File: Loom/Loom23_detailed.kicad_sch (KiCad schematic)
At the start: 7 parts

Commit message: Changes to the injector numbering
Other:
- sheet Relaybox indicators renamed Relaybox indicators (relays)
- added sheet Relaybox indicators (ECU) (Relaybox Indicator LEDs/relaybox_indicator_leds.kicad_sch)
- note added: "High impedance injectors, no extra resistors needed."
- note added: "Note: there is only one relaybox indicator board, but it can be connected to either the relays or the ECU, so it is included twice in this diagram"
- note removed: "Assuming cylinder 1 is on the left High impedance injectors, no extra resistors needed."
- note removed: "CAN Bus"
- note removed: "CAN Sensors"

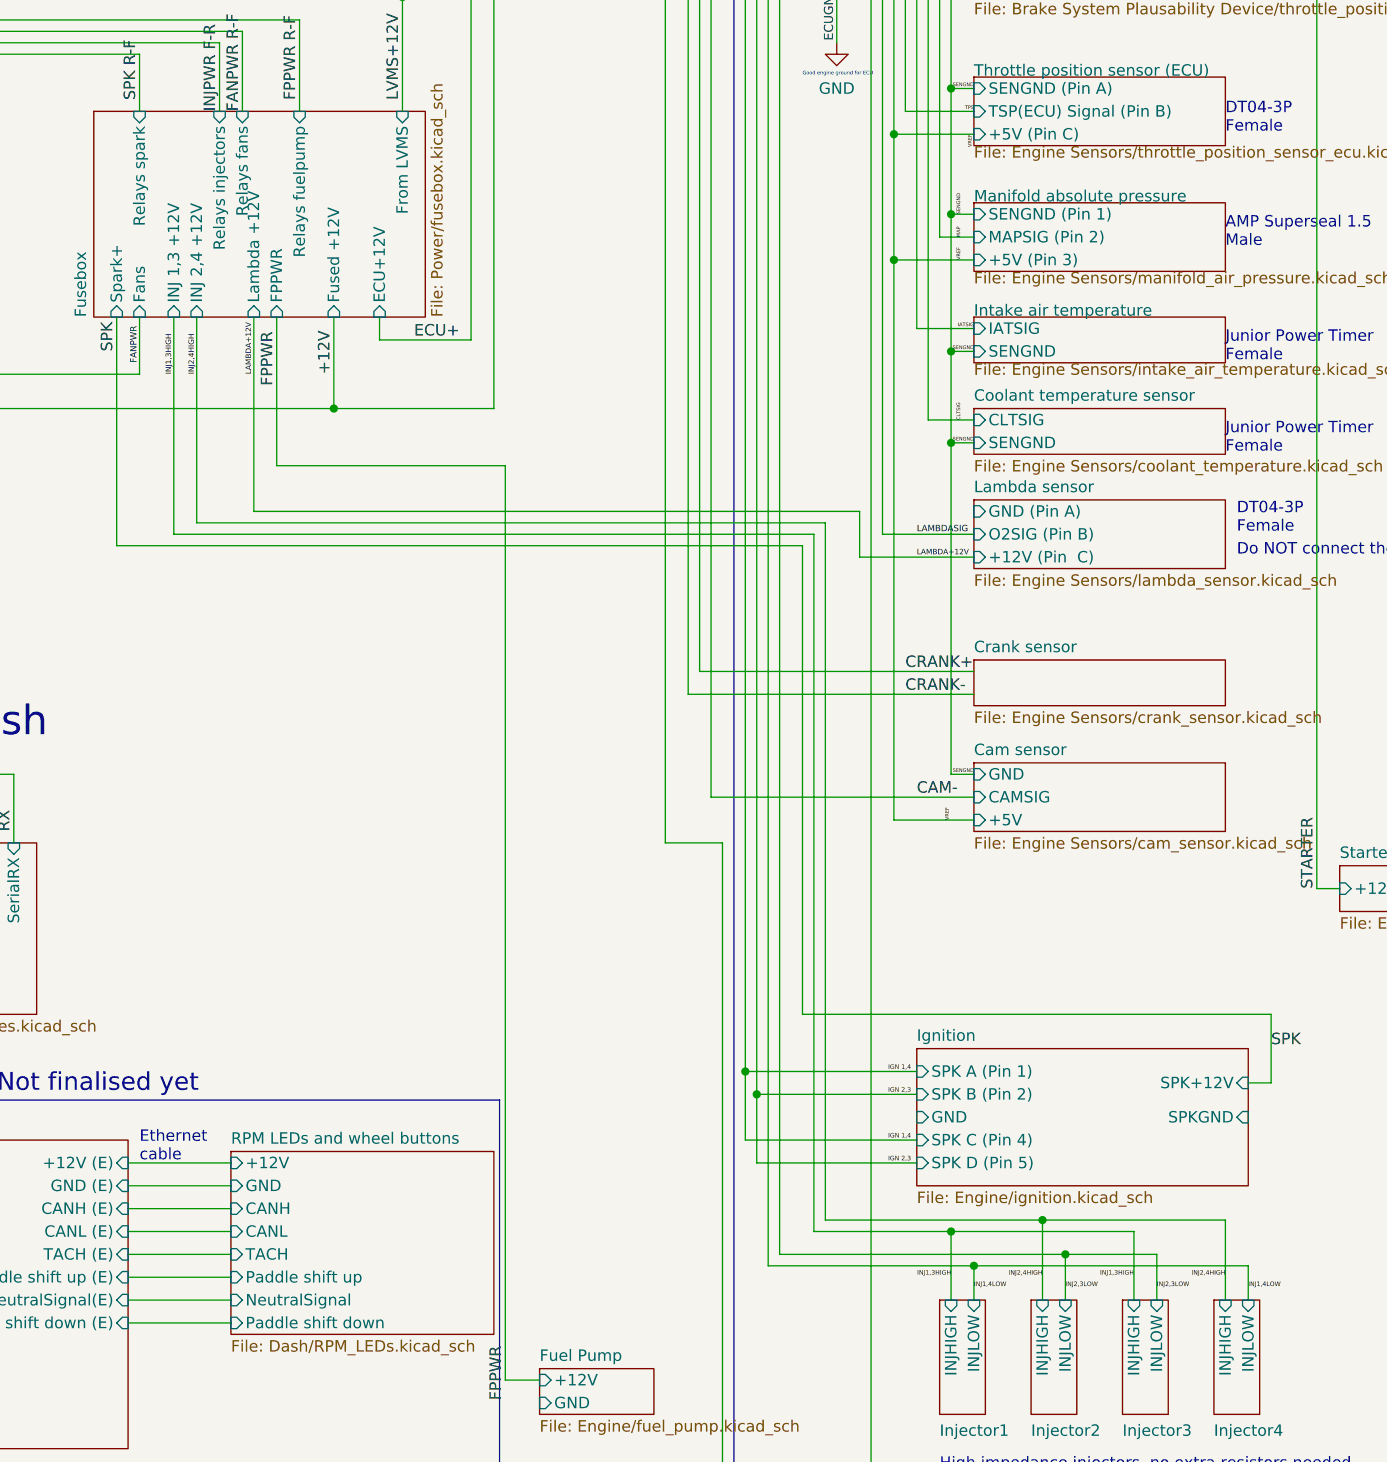
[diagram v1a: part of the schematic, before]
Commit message: Fixed injector high side labels
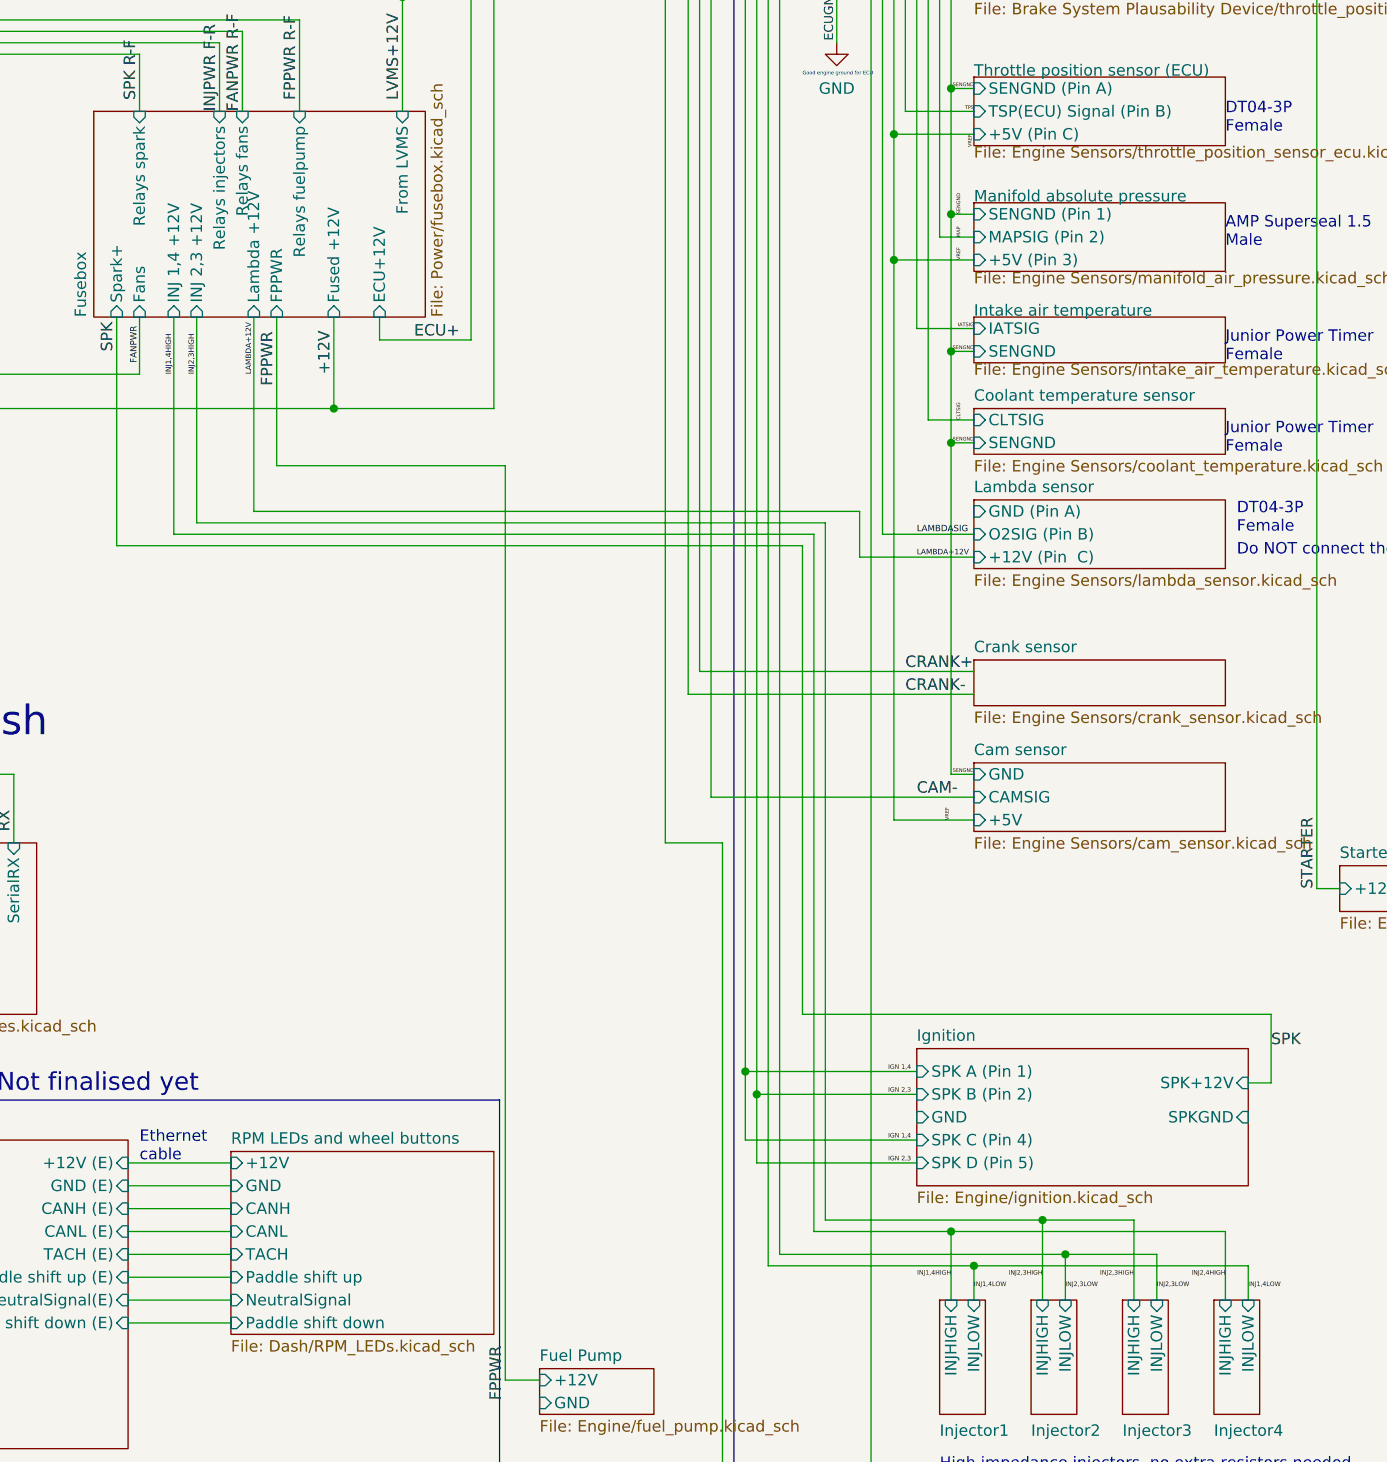
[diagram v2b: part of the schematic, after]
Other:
- sheet Fusebox ports: added INJ 1,4 +12V, INJ 2,3 +12V; removed INJ 1,3 +12V, INJ 2,4 +12V
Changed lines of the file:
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@@
     (stroke (width 0) (type default) (color 0 255 0 1))
   )
-  (wire (pts (xy 402.59 224.79) (xy 402.59 232.41))
+  (wire (pts (xy 402.59 223.52) (xy 402.59 232.41))
     (stroke (width 0) (type default))
   )
@@
     (stroke (width 0) (type default) (color 0 255 0 1))
   )
-  (wire (pts (xy 392.43 223.52) (xy 412.75 223.52))
+  (wire (pts (xy 392.43 223.52) (xy 402.59 223.52))
     (stroke (width 0) (type default))
   )
@@
     (stroke (width 0) (type default))
   )
-  (wire (pts (xy 382.27 224.79) (xy 402.59 224.79))
+  (wire (pts (xy 382.27 224.79) (xy 412.75 224.79))
     (stroke (width 0) (type default))
   )
@@
     (stroke (width 0) (type default) (color 0 255 0 1))
   )
+  (wire (pts (xy 412.75 224.79) (xy 412.75 232.41))
+    (stroke (width 0) (type default))
+  )
   (wire (pts (xy 313.69 133.35) (xy 233.68 133.35))
     (stroke (width 0) (type default))
@@
     (stroke (width 0) (type default))
   )
-  (wire (pts (xy 412.75 223.52) (xy 412.75 232.41))
-    (stroke (width 0) (type default))
-  )
   (wire (pts (xy 254 103.505) (xy 254 146.05))
     (stroke (width 0) (type default))
@@
     (effects (font (size 1.27 1.27)) (justify left bottom))
   )
-  (label "INJ2,4HIGH" (at 392.43 229.87 180) (fields_autoplaced)
+  (label "INJ2,3HIGH" (at 392.43 229.87 180) (fields_autoplaced)
     (effects (font (size 0.5 0.5)) (justify right bottom))
   )
@@
     (effects (font (size 1.27 1.27)) (justify left bottom))
   )
-  (label "INJ1,3HIGH" (at 382.27 229.87 180) (fields_autoplaced)
+  (label "INJ1,4HIGH" (at 382.27 229.87 180) (fields_autoplaced)
     (effects (font (size 0.5 0.5)) (justify right bottom))
   )
@@
     (effects (font (size 1.27 1.27)) (justify left bottom))
   )
-  (label "INJ1,3HIGH" (at 402.59 229.87 180) (fields_autoplaced)
+  (label "INJ2,3HIGH" (at 402.59 229.87 180) (fields_autoplaced)
     (effects (font (size 0.5 0.5)) (justify right bottom))
   )
-  (label "INJ2,4HIGH" (at 298.45 129.54 90) (fields_autoplaced)
+  (label "INJ2,3HIGH" (at 298.45 129.54 90) (fields_autoplaced)
     (effects (font (size 0.6 0.6)) (justify left bottom))
   )
@@
     (effects (font (size 1.27 1.27)) (justify left bottom))
   )
-  (label "INJ1,3HIGH" (at 295.91 129.54 90) (fields_autoplaced)
+  (label "INJ1,4HIGH" (at 295.91 129.54 90) (fields_autoplaced)
     (effects (font (size 0.6 0.6)) (justify left bottom))
   )
@@
       (effects (font (size 1.27 1.27)) (justify left))
     )
-    (pin "INJ 2,4 +12V" input (at 298.45 123.19 270)
+    (pin "INJ 2,3 +12V" input (at 298.45 123.19 270)
       (effects (font (size 1.27 1.27)) (justify left))
     )
-    (pin "INJ 1,3 +12V" input (at 295.91 123.19 270)
+    (pin "INJ 1,4 +12V" input (at 295.91 123.19 270)
       (effects (font (size 1.27 1.27)) (justify left))
     )
